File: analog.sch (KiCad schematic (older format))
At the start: 102 parts, among them J10 Conn_01x02_Female, J11 Conn_01x02_Male, J12 Conn_01x02_Male, J13 Conn_01x02_Female, J14 Conn_01x02_Male, J15 Conn_01x02_Female, J4 Conn_01x04_Male, J5 Conn_01x04_Male, J8 Conn_01x02_Male, J9 Conn_01x02_Female, Q1 BSS123, Q2 BSS123, U13 LP2985-3.3, U14 AD8039, U15 AD8039, U17 MAX1932, U18 MAX1932, U19 AD8039

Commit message: added esp header and cw psu
footpints and board layouts to do
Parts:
- added C100, C101, C102, C103, C104, C105, C106, C107, C108, C109, C110, C80, C81, C82, C83, C84, C85, C86, C87, C88, C89, C90, C91, C92, C93, C94, C96, C97, C98, C99: 10u, Capacitor_SMD:C_1206_3216Metric, symbol Device:C
- added C111, C95: 10n, Capacitor_SMD:C_1206_3216Metric, symbol Device:C
- added D11, D12, D13, D14, D15, D16, D17, D18, D19, D20, D21, D22, D23, D24: BAT54SW, Package_TO_SOT_SMD:SOT-323_SC-70, symbol Diode:BAT54SW
- added Q3, Q4: BSS123, Package_TO_SOT_SMD:SOT-23, symbol Transistor_FET:BSS123
- added R72, R74, R75, R77: 10k, Resistor_SMD:R_0603_1608Metric, symbol Device:R
- added R73, R76: 180, Resistor_SMD:R_0603_1608Metric, symbol Device:R
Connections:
- net +5V: now also R73.2, R76.2
- net GND: now also C110.2, C111.2, C80.2, C94.2, C95.2, C96.2
- net GNDREF: now also C43.1, C44.1, C49.1, C50.1; no longer C43.2, C44.2, C49.2, C50.2
- net VBIAS1: now also R77.2
- net VBIAS2: now also R74.2
- net V_OFFSET: now also C43.2, C44.2, C49.2, C50.2; no longer C43.1, C44.1, C49.1, C50.1
- new net: C97.1, D18.1, Q4.3 (D), R76.1
- new net: C97.2, C99.1, D18.2, D19.1
- new net: C96.1, C98.2, D18.3
- new net: C101.1, C99.2, D19.2, D20.1
- new net: C100.2, C98.1, D19.3
- new net: C101.2, C103.1, D20.2, D21.1
- new net: C100.1, C102.2, D20.3
- new net: C103.2, C105.1, D21.2, D22.1
- new net: C102.1, C104.2, D21.3
- new net: C105.2, C107.1, D22.2, D23.1
- new net: C104.1, C106.2, D22.3
- new net: C107.2, C109.1, D23.2, D24.1
- new net: C106.1, C108.2, D23.3
- new net: C109.2, C110.1, C111.1, D24.2, R77.1
- new net: C108.1, D24.3
- new net: C81.1, D11.1, Q3.3 (D), R73.1
- new net: C81.2, C83.1, D11.2, D12.1
- new net: C80.1, C82.2, D11.3
- new net: C83.2, C85.1, D12.2, D13.1
- new net: C82.1, C84.2, D12.3
- new net: C85.2, C87.1, D13.2, D14.1
- new net: C84.1, C86.2, D13.3
- new net: C87.2, C89.1, D14.2, D15.1
- new net: C86.1, C88.2, D14.3
- new net: C89.2, C91.1, D15.2, D16.1
- new net: C88.1, C90.2, D15.3
- new net: C91.2, C93.1, D16.2, D17.1
- new net: C90.1, C92.2, D16.3
- new net: C93.2, C94.1, C95.1, D17.2, R74.1
- new net: C92.1, D17.3
- new net +3V3: Q3.1 (G), Q4.1 (G), R72.2, R75.2
- new net PSU_A_DRIVE: Q4.2 (S), R75.1
- new net PSU_B_DRIVE: Q3.2 (S), R72.1
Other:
- note added: "CW PSU - prototype"
- note added: "Cockcroft Walton Power supplies added.\nThese will be DNP in this production run."
- moved on the sheet: C37, C40, C43, C44, C46, C48, C49, C50, C52, C53, C54, D6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

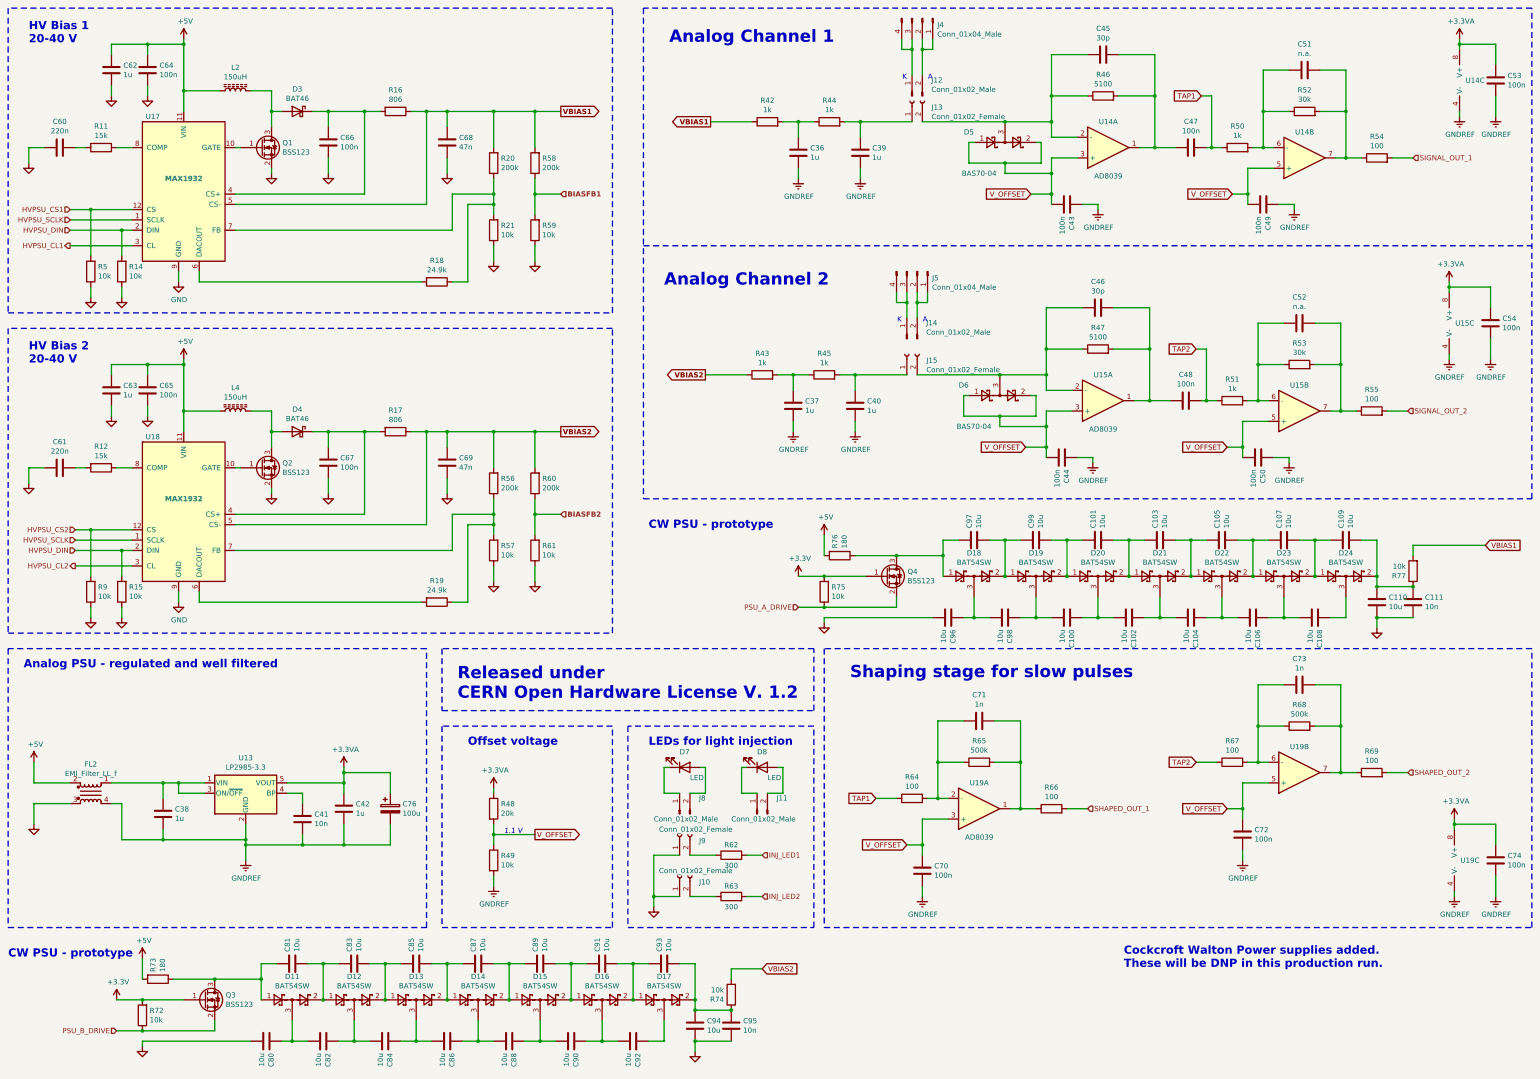
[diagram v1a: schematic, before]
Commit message: footprints corrected, routing in progress
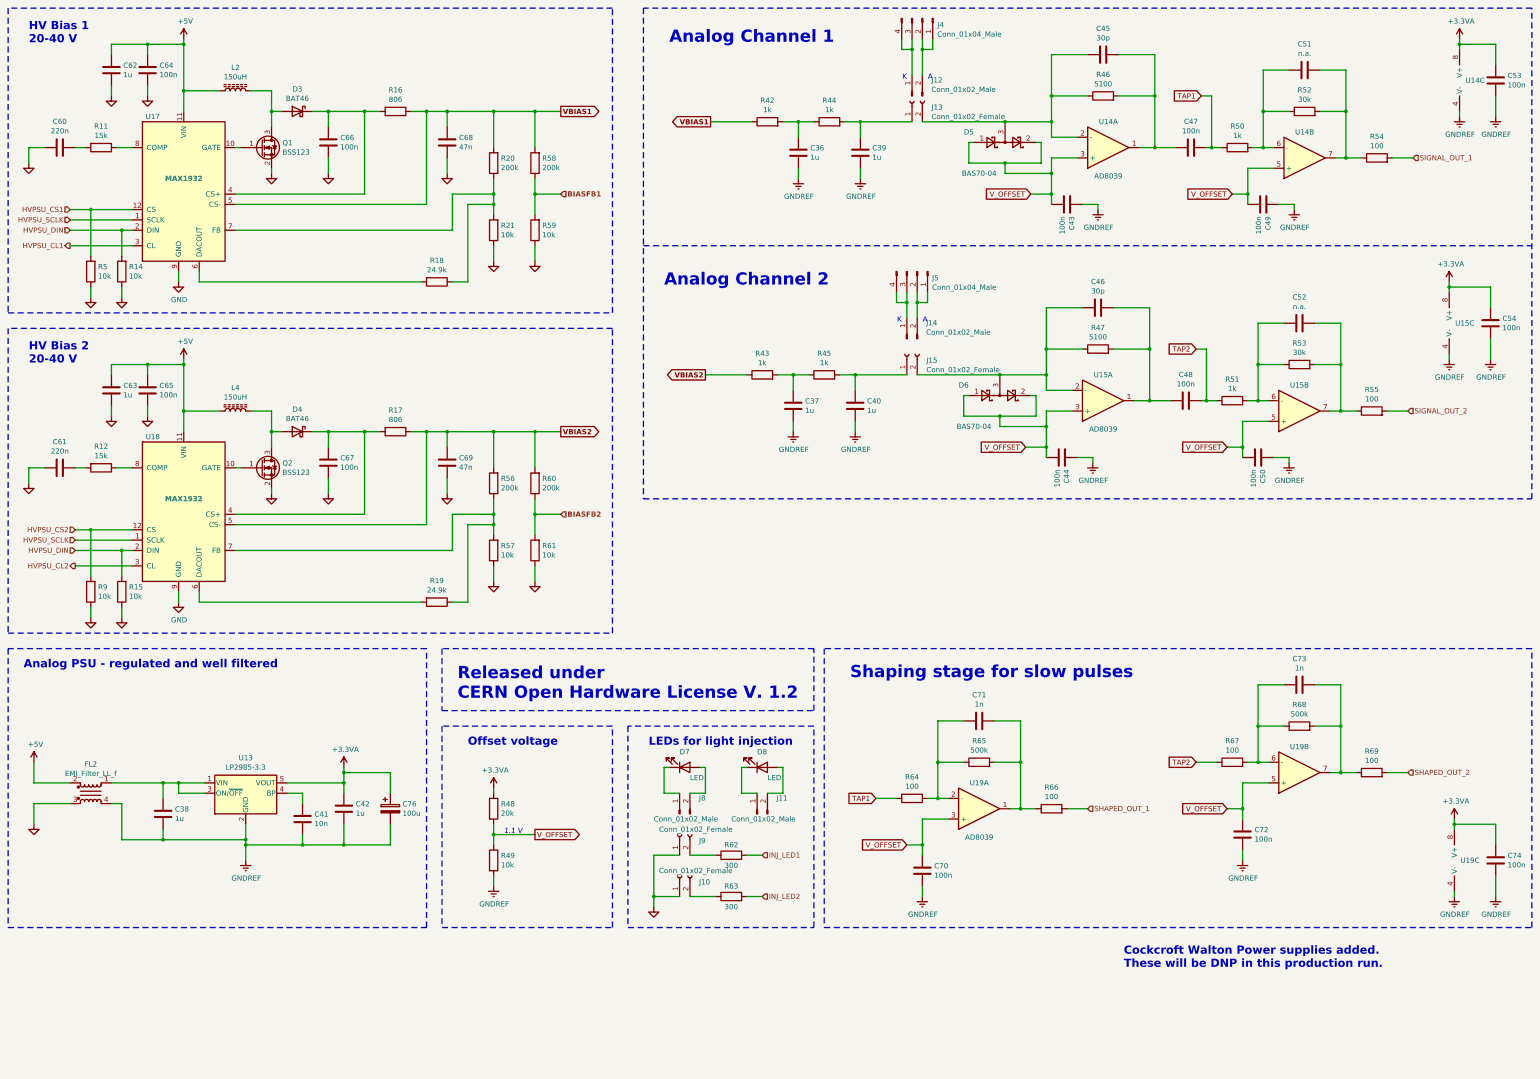
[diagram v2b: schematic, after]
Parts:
- removed C100, C101, C102, C103, C104, C105, C106, C107, C108, C109, C110, C80, C81, C82, C83, C84, C85, C86, C87, C88, C89, C90, C91, C92, C93, C94, C96, C97, C98, C99: 10u, Capacitor_SMD:C_1206_3216Metric, symbol Device:C
- removed C111, C95: 10n, Capacitor_SMD:C_1206_3216Metric, symbol Device:C
- removed D11, D12, D13, D14, D15, D16, D17, D18, D19, D20, D21, D22, D23, D24: BAT54SW, Package_TO_SOT_SMD:SOT-323_SC-70, symbol Diode:BAT54SW
- removed Q3, Q4: BSS123, Package_TO_SOT_SMD:SOT-23, symbol Transistor_FET:BSS123
- removed R72, R74, R75, R77: 10k, Resistor_SMD:R_0603_1608Metric, symbol Device:R
- removed R73, R76: 180, Resistor_SMD:R_0603_1608Metric, symbol Device:R
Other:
- note removed: "CW PSU - prototype"
